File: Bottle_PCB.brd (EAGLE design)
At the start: 100 x 50 mm, 106 parts, among them J1 GROVE-4P-2.0-SMD, Q1 8.000 MHz, Q2 ZVN 3306 F, Q3 ZVN 3306 F, Q4 ZVN 3306 F, Q5 ZVN 3306 F, Q6 ZVN 3306 F, Q7 ZVN 3306 F, U1 USD-SOCKETNEW

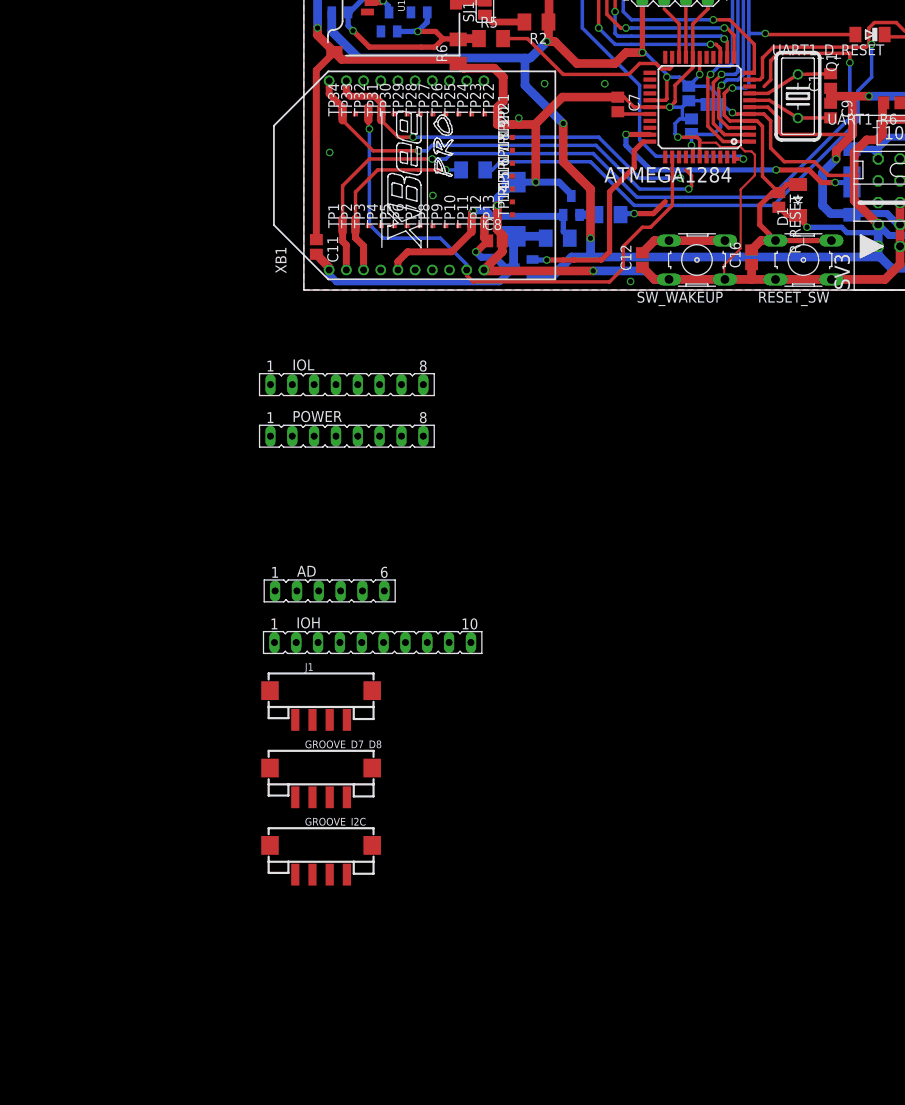
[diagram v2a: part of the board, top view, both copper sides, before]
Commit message: - changed old BTBee Pro specific socketing into more generic XBEE socket
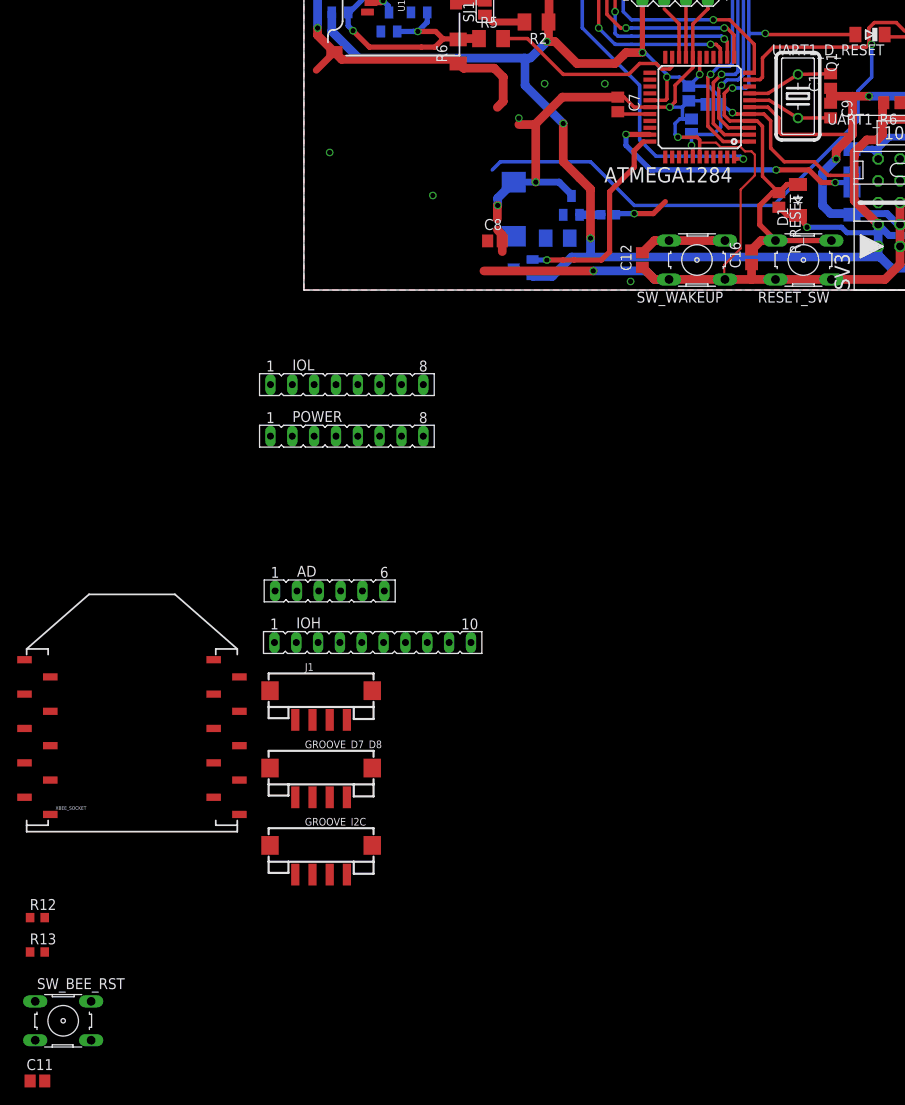
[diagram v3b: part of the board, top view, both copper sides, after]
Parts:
- removed R9: 2k, rcl:M1206
- removed TP1, TP10, TP11, TP12, TP13, TP14, TP15, TP16, TP17, TP18, TP19, TP2, TP20, TP21, TP22, TP23, TP24, TP25, TP26, TP27, TP28, TP29, TP3, TP30, TP31, TP32, TP33, TP34, TP4, TP5, TP6, TP7, TP8, TP9: TPTP06SQ, testpad:TP06SQ
- removed XB1: XBEE-PRO, maxstream:XBEE-PRO
- added R12, R13: 4k7, resistor:R0603
- added SW_BEE_RST: (no value), switch-omron:B3F-10XX
- added XBEE_SOCKET: XBEE-1B3, SparkFun-RF:XBEE-SMD
- R8: device rcl:M1206 -> resistor:R0603
- moved C11 102.3 mm to (-31.0, -92.0), turned to 0 degrees
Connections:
- net BT_RESET renamed BEE_RESET_SIGNAL
- net BT_VCC_SIGNAL renamed BEE_VCC_SIGNAL
- removed net BT_MODE: TP34.TP, XB1.20
- removed net BT_PAIR: TP32.TP, XB1.9
- removed net BT_RESET_TRANSISTOR: Q6.2, R7.1, TP11.TP, XB1.5
- removed net BT_STATUS: TP31.TP, XB1.19
- removed net BT_VCC: C10.+, C11.2, C8.1, Q7.3, R7.2, TP12.TP, XB1.1
- removed net USB_BT_TXD0_RES: R9.1, TP2.TP, XB1.3
- new net BEE_MODE: XBEE_SOCKET.20
- new net BEE_PAIR: XBEE_SOCKET.9
- new net BEE_RESET: C11.2, Q6.2, R7.1, SW_BEE_RST.1, SW_BEE_RST.2, XBEE_SOCKET.5
- new net BEE_STATUS: XBEE_SOCKET.19
- new net BEE_VCC: C10.+, C8.1, Q7.3, R7.2, XBEE_SOCKET.1
- new net N$15: R13.2, XBEE_SOCKET.3
- new net N$8: R12.2, XBEE_SOCKET.2
- net GND: now also SW_BEE_RST.3, SW_BEE_RST.4, XBEE_SOCKET.10; no longer TP13.TP, TP21.TP, TP22.TP, XB1.10
- net PD0_RXD0_USB: now also R12.1
- net PD0_RXD0_USB_BT: no longer TP1.TP, XB1.2
- net PD1_TXD0_USB: now also R13.1; no longer R9.2
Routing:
- net PD0_RXD0_USB_BT: track 96.9 -> 0.00 mm, vias 2 -> 0
- net BT_PAIR: track 63.2 -> 0.00 mm, vias 1 -> 0
- net BT_MODE: track 52.0 -> 0.00 mm, vias 2 -> 0
- net BT_STATUS: track 45.8 -> 0.00 mm, vias 2 -> 0
- net BT_VCC: track 42.6 -> 0.00 mm, vias 1 -> 0
- net GND: track 456.6 -> 428.0 mm
- net BT_RESET_TRANSISTOR: track 27.3 -> 0.00 mm, vias 1 -> 0
- net USB_BT_TXD0_RES: track 22.8 -> 0.00 mm, vias 1 -> 0
- net PD1_TXD0_USB: track 84.9 -> 84.1 mm
- net N$34: track 1.98 -> 2.53 mm

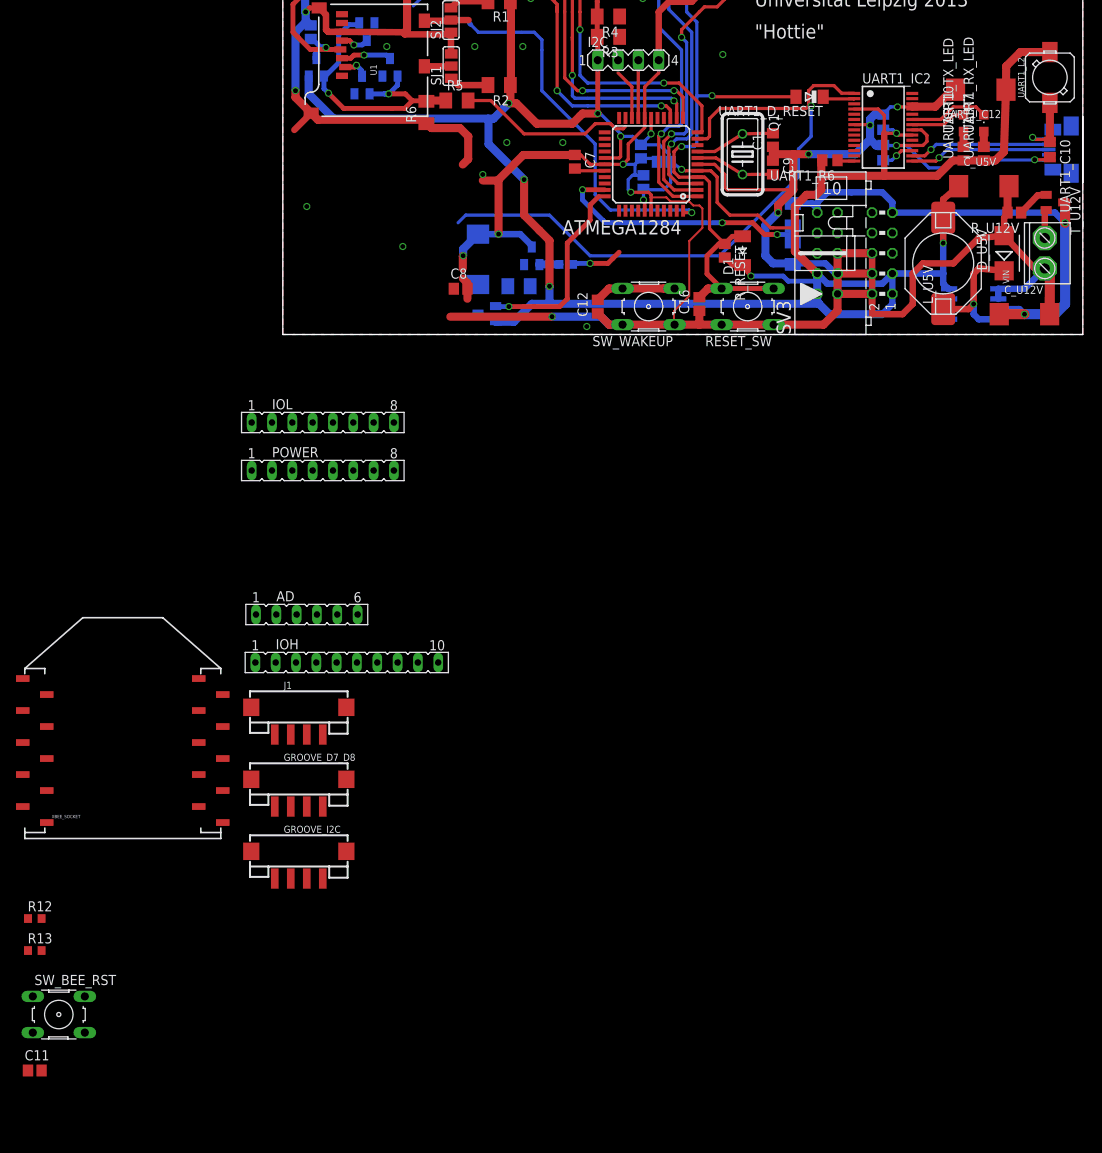
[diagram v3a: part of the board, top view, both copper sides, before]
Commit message: - added FTDI serial connector - employed sparkfun lib for connectors
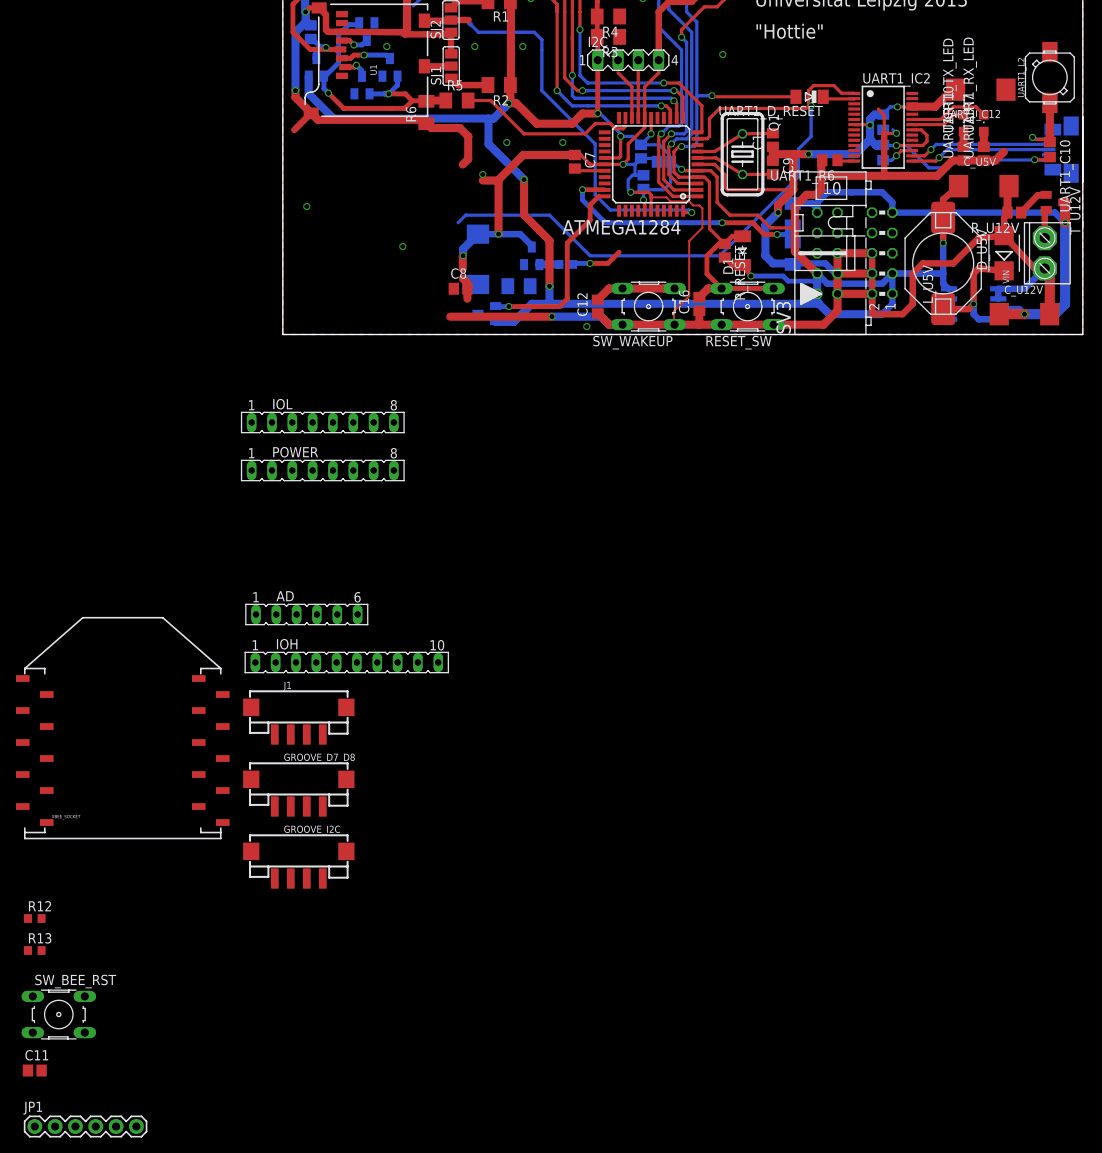
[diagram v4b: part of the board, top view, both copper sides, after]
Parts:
- added JP1: (no value), SparkFun-Connectors:1X06
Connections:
- net RESET renamed MCU_RST
- removed net DTR#: UART1_D_RESET.C, UART1_IC2.2
- new net FTDI_CTS: JP1.CTS, UART1_IC2.11
- new net FTDI_DTR: JP1.DTR, UART1_D_RESET.C, UART1_IC2.2
- net +3V3: now also JP1.VCC; no longer UART1_C11.1, UART1_C12.+, UART1_IC2.20, UART1_L2.2
- net +5V: now also UART1_C11.1, UART1_C12.+, UART1_IC2.20, UART1_L2.2
- net GND: now also JP1.GND
- net PD0_RXD0_USB: now also JP1.TXO
- net PD1_TXD0_USB: now also JP1.RXI
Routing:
- net +3V3: track 344.1 -> 321.3 mm
- net FTDI_DTR: track 0.00 -> 4.01 mm
- net DTR#: track 4.01 -> 0.00 mm
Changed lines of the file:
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@@
 </element>
 <element name="C11" library="quantum-sensor" package="C0805" value="100n" x="-31" y="-92"/>
+<element name="JP1" library="SparkFun-Connectors" package="1X06" value="" x="-31" y="-99"/>
 </elements>
 <signals>
@@
 <contactref element="SW_BEE_RST" pad="4"/>
 <contactref element="XBEE_SOCKET" pad="10"/>
+<contactref element="JP1" pad="GND"/>
 <wire x1="-31.2512" y1="-87.2606" x2="-31.85" y2="-92" width="0" layer="19" extent="1-1"/>
 <wire x1="-24.7488" y1="-87.2606" x2="-31.2512" y2="-87.2606" width="0" layer="19" extent="1-1"/>
+<wire x1="-18.3" y1="-99" x2="-24.7488" y2="-87.2606" width="0" layer="19" extent="1-1"/>
 <wire x1="-29.5" y1="-61" x2="-31.2512" y2="-87.2606" width="0" layer="19" extent="1-1"/>
 <wire x1="-1" y1="-59" x2="-29.5" y2="-61" width="0" layer="19" extent="1-1"/>
@@
 <wire x1="54.1275" y1="22.0725" x2="57.4675" y2="20.0025" width="0.4064" layer="1"/>
 </signal>
-<signal name="RESET">
+<signal name="MCU_RST">
 <contactref element="ATMEGA1284" pad="4"/>
 <contactref element="R_RESET" pad="1"/>
@@
 <wire x1="83.854" y1="27.466" x2="85.09" y2="27.466" width="0.4064" layer="1"/>
 </signal>
-<signal name="DTR#">
+<signal name="FTDI_DTR">
 <contactref element="UART1_IC2" pad="2"/>
 <contactref element="UART1_D_RESET" pad="C"/>
@@
 <wire x1="71.3985" y1="29.4495" x2="67.818" y2="29.4495" width="0.4064" layer="1"/>
 <wire x1="67.818" y1="29.4495" x2="67.5495" y2="29.718" width="0.4064" layer="1"/>
+<contactref element="JP1" pad="DTR"/>
+<wire x1="67.818" y1="29.4495" x2="-31" y2="-99" width="0" layer="19" extent="1-1"/>
 </signal>
 <signal name="N$18">
@@
 <contactref element="R_RESET" pad="2"/>
 <contactref element="D1" pad="C"/>
-<contactref element="UART1_IC2" pad="20"/>
-<contactref element="UART1_IC2" pad="4"/>
-<contactref element="UART1_C12" pad="+"/>
-<contactref element="UART1_C11" pad="1"/>
-<contactref element="UART1_L2" pad="2"/>
 <contactref element="ATMEGA1284" pad="27"/>
 <contactref element="ATMEGA1284" pad="38"/>
@@
 <contactref element="UART1_R7" pad="1"/>
 <contactref element="UART1_R6" pad="2"/>
-<wire x1="78.682" y1="24.933" x2="76.921" y2="24.933" width="0.4064" layer="1"/>
 <wire x1="76.921" y1="24.933" x2="76.708" y2="25.146" width="0.4064" layer="1"/>
 <via x="76.708" y="25.146" extent="1-16" drill="0.6"/>
 <wire x1="76.708" y1="25.146" x2="76.261" y2="25.593" width="0.4064" layer="16"/>
-<wire x1="76.261" y1="25.593" x2="75.057" y2="25.593" width="0.4064" layer="16"/>
 <wire x1="85.09" y1="21.756" x2="87.63" y2="21.756" width="1.016" layer="1"/>
-<wire x1="95.885" y1="35.306" x2="92.202" y2="35.306" width="1.016" layer="1"/>
-<wire x1="92.202" y1="35.306" x2="90.424" y2="33.528" width="1.016" layer="1"/>
-<wire x1="90.424" y1="33.528" x2="90.399" y2="30.607" width="1.016" layer="1"/>
 <wire x1="74.93" y1="2.54" x2="68.326" y2="2.54" width="1.016" layer="16"/>
 <wire x1="68.326" y1="2.54" x2="67.02425" y2="3.84175" width="1.016" layer="16"/>
@@
 <wire x1="81.8185" y1="19.8425" x2="75.184" y2="19.8425" width="1.016" layer="1"/>
 <wire x1="75.184" y1="19.8425" x2="67.31" y2="19.8425" width="1.016" layer="1"/>
-<wire x1="71.432" y1="28.183" x2="74.433" y2="28.183" width="0.4064" layer="1"/>
 <wire x1="74.433" y1="28.183" x2="75.184" y2="27.432" width="0.4064" layer="1"/>
 <wire x1="76.708" y1="25.146" x2="75.184" y2="25.146" width="0.4064" layer="1"/>
@@
 <wire x1="87.63" y1="21.756" x2="89.066" y2="21.756" width="1.016" layer="1"/>
 <wire x1="89.066" y1="21.756" x2="90.145" y2="22.835" width="1.016" layer="1"/>
-<wire x1="90.399" y1="30.607" x2="90.145" y2="22.835" width="1.016" layer="1"/>
 <wire x1="51.8375" y1="20.4725" x2="53.505" y2="20.4725" width="0.4064" layer="1"/>
 <wire x1="53.505" y1="20.4725" x2="54.2925" y2="19.685" width="0.4064" layer="1"/>
@@
 <contactref element="GROOVE_D7_D8" pad="2"/>
 <contactref element="J1" pad="2"/>
+<contactref element="UART1_IC2" pad="4"/>
+<contactref element="JP1" pad="VCC"/>
+<wire x1="1" y1="-68" x2="-23.38" y2="-99" width="0" layer="19" extent="1-1"/>
 <wire x1="1" y1="-59" x2="1" y2="-68" width="0" layer="19" extent="1-1"/>
 <wire x1="1" y1="-50" x2="1" y2="-59" width="0" layer="19" extent="1-1"/>
 <wire x1="3.73" y1="-17" x2="1" y2="-50" width="0" layer="19" extent="1-1"/>
 <wire x1="26.595" y1="1.6535" x2="3.73" y2="-17" width="0" layer="19" extent="16-16"/>
+<wire x1="71.432" y1="28.183" x2="74.433" y2="28.183" width="0" layer="19" extent="1-1"/>
 </signal>
 <signal name="N$16">
@@
 <contactref element="UART1_IC2" pad="1"/>
 <contactref element="R13" pad="1"/>
+<contactref element="JP1" pad="RXI"/>
+<wire x1="-31.85" y1="-77" x2="-28.46" y2="-99" width="0" layer="19" extent="1-1"/>
 <wire x1="-1.35" y1="-11" x2="-31.85" y2="-77" width="0" layer="19" extent="1-1"/>
 <wire x1="21.9075" y1="13.97" x2="-1.35" y2="-11" width="0" layer="19" extent="16-16"/>
@@
 <contactref element="UART1_IC2" pad="5"/>
 <contactref element="R12" pad="1"/>
+<contactref element="JP1" pad="TXO"/>
+<wire x1="-31.85" y1="-73" x2="-25.92" y2="-99" width="0" layer="19" extent="1-1"/>
 <wire x1="51.8375" y1="23.6725" x2="-31.85" y2="-73" width="0" layer="19" extent="1-1"/>
 <wire x1="71.432" y1="27.533" x2="51.8375" y2="23.6725" width="0" layer="19" extent="1-1"/>
@@
 <contactref element="POWER" pad="5"/>
 <contactref element="POWER" pad="2"/>
-<wire x1="6.27" y1="-17" x2="-1.35" y2="-17" width="0" layer="19" extent="1-1"/>
+<contactref element="UART1_C11" pad="1"/>
+<contactref element="UART1_C12" pad="+"/>
+<contactref element="UART1_IC2" pad="20"/>
+<contactref element="UART1_L2" pad="2"/>
+<wire x1="90.399" y1="30.607" x2="95.885" y2="35.306" width="0" layer="19" extent="1-1"/>
+<wire x1="78.682" y1="24.933" x2="90.399" y2="30.607" width="0" layer="19" extent="1-1"/>
+<wire x1="75.057" y1="25.593" x2="78.682" y2="24.933" width="0" layer="19" extent="1-16"/>
+<wire x1="6.27" y1="-17" x2="75.057" y2="25.593" width="0" layer="19" extent="16-16"/>
+<wire x1="-1.35" y1="-17" x2="6.27" y2="-17" width="0" layer="19" extent="1-1"/>
 </signal>
 <signal name="PA6">
@@
 <contactref element="XBEE_SOCKET" pad="9"/>
 </signal>
+<signal name="FTDI_CTS">
+<contactref element="UART1_IC2" pad="11"/>
+<contactref element="JP1" pad="CTS"/>
+<wire x1="71.432" y1="23.633" x2="-20.84" y2="-99" width="0" layer="19" extent="1-1"/>
+</signal>
 </signals>
